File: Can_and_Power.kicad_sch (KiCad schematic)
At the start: 8 parts, among them J2 776280-1, J3 776280-1, U12 MCP2562-E_SN, U3 MCP2562-E_SN

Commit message: Finished routing
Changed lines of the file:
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@@
+	(wire
+		(pts
+			(xy 68.58 45.72) (xy 67.31 45.72)
+		)
+		(stroke
+			(width 0)
+			(type default)
+		)
+	)
 	(wire
 		(pts
@@
 	(symbol
 		(lib_id "power:PWR_FLAG")
-		(at 67.31 45.72 270)
+		(at 68.58 45.72 270)
 		(unit 1)
 		(exclude_from_sim no)
@@
 		(fields_autoplaced yes)
 		(property "Reference" "#FLG02"
-			(at 69.215 45.72 0)
+			(at 70.485 45.72 0)
 			(effects
 				(font
@@
 		)
 		(property "Value" "PWR_FLAG"
-			(at 71.12 45.7199 90)
+			(at 72.39 45.7199 90)
 			(effects
 				(font
@@
 		)
 		(property "Footprint" ""
-			(at 67.31 45.72 0)
+			(at 68.58 45.72 0)
 			(effects
 				(font
@@
 		)
 		(property "Datasheet" "~"
-			(at 67.31 45.72 0)
+			(at 68.58 45.72 0)
 			(effects
 				(font
@@
 		)
 		(property "Description" "Special symbol for telling ERC where power comes from"
-			(at 67.31 45.72 0)
-			(effects
-				(font
+			(at 68.58 45.72 0)
+			(effects
+				(font

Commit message: Finalized analog components. Everything is done 🙏
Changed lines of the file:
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@@
-	)
-	(junction
-		(at 67.31 45.72)
-		(diameter 0)
-		(color 0 0 0 0)
 	)
 	(junction
@@
 	(wire
 		(pts
-			(xy 68.58 45.72) (xy 67.31 45.72)
-		)
-		(stroke
-			(width 0)
-			(type default)
-		)
-	)
-	(wire
-		(pts
 			(xy 220.98 110.49) (xy 220.98 114.3)
 		)
@@
 	(wire
 		(pts
-			(xy 67.31 45.72) (xy 67.31 54.61)
-		)
-		(stroke
-			(width 0)
-			(type default)
-		)
-	)
-	(wire
-		(pts
 			(xy 121.92 69.85) (xy 121.92 111.76)
 		)
@@
 	(wire
 		(pts
-			(xy 67.31 41.91) (xy 67.31 45.72)
+			(xy 67.31 41.91) (xy 67.31 54.61)
 		)
 		(stroke
@@
 					(unit 1)
 				)
-			)
-		)
-	)
-	(symbol
-		(lib_id "power:PWR_FLAG")
-		(at 68.58 45.72 270)
-		(unit 1)
-		(exclude_from_sim no)
-		(in_bom yes)
-		(on_board yes)
-		(dnp no)
-		(fields_autoplaced yes)
-		(property "Reference" "#FLG02"
-			(at 70.485 45.72 0)
-			(effects
-				(font
-					(size 1.27 1.27)
-				)
-				(hide yes)
-			)
-		)
-		(property "Value" "PWR_FLAG"
-			(at 72.39 45.7199 90)
-			(effects
-				(font
-					(size 1.27 1.27)
-				)
-				(justify left)
-			)
-		)
-		(property "Footprint" ""
-			(at 68.58 45.72 0)
-			(effects
-				(font
-					(size 1.27 1.27)
-				)
-				(hide yes)
-			)
-		)
-		(property "Datasheet" "~"
-			(at 68.58 45.72 0)
-			(effects
-				(font
-					(size 1.27 1.27)
-				)
-				(hide yes)
-			)
-		)
-		(property "Description" "Special symbol for telling ERC where power comes from"
-			(at 68.58 45.72 0)
-			(effects
-				(font
-					(size 1.27 1.27)
-				)
-				(hide yes)
-			)
-		)
-		(pin "1"
-		)
-		(instances
-			(project "Main-Board-V2"
-				(path "/c01682a2-308a-4674-9b8f-80e441c05d08/2eeb5b34-c445-4914-b41b-f611e24c0c64"
-					(reference "#FLG02")
-					(unit 1)
-				)

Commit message: Added fuse, switch to horizontal connecotor, redid all routing
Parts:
- added F1: Fuse, Fuse:Fuse_0805_2012Metric, symbol Device:Fuse
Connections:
- net +12V: now also F1.2; no longer J2.1, J3.1
- new net: F1.1, J2.1, J3.1

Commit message: added LED indicators, fixed footprints
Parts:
- C4, C5, C8, C9: footprint GRT155C80J105KE01J:CAPC1005X55N -> Capacitor_SMD:C_0805_2012Metric
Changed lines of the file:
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@@
 			)
 		)
-		(property "Footprint" "GRT155C80J105KE01J:CAPC1005X55N"
+		(property "Footprint" "Capacitor_SMD:C_0805_2012Metric"
 			(at 233.68 53.6448 0)
 			(effects
@@
 			)
 		)
-		(property "Footprint" "GRT155C80J105KE01J:CAPC1005X55N"
+		(property "Footprint" "Capacitor_SMD:C_0805_2012Metric"
 			(at 240.03 109.5248 0)
 			(effects
@@
 			)
 		)
-		(property "Footprint" "GRT155C80J105KE01J:CAPC1005X55N"
+		(property "Footprint" "Capacitor_SMD:C_0805_2012Metric"
 			(at 245.11 53.6448 0)
 			(effects
@@
 			)
 		)
-		(property "Footprint" "GRT155C80J105KE01J:CAPC1005X55N"
+		(property "Footprint" "Capacitor_SMD:C_0805_2012Metric"
 			(at 228.6 109.5248 0)
 			(effects

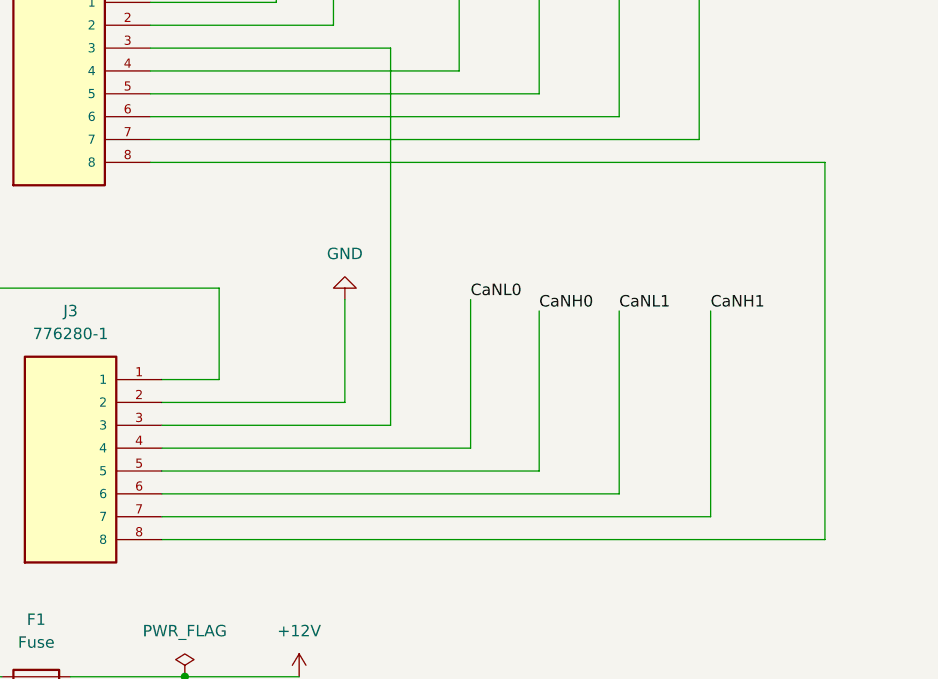
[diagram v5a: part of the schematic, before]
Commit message: redid 35 pos pinout
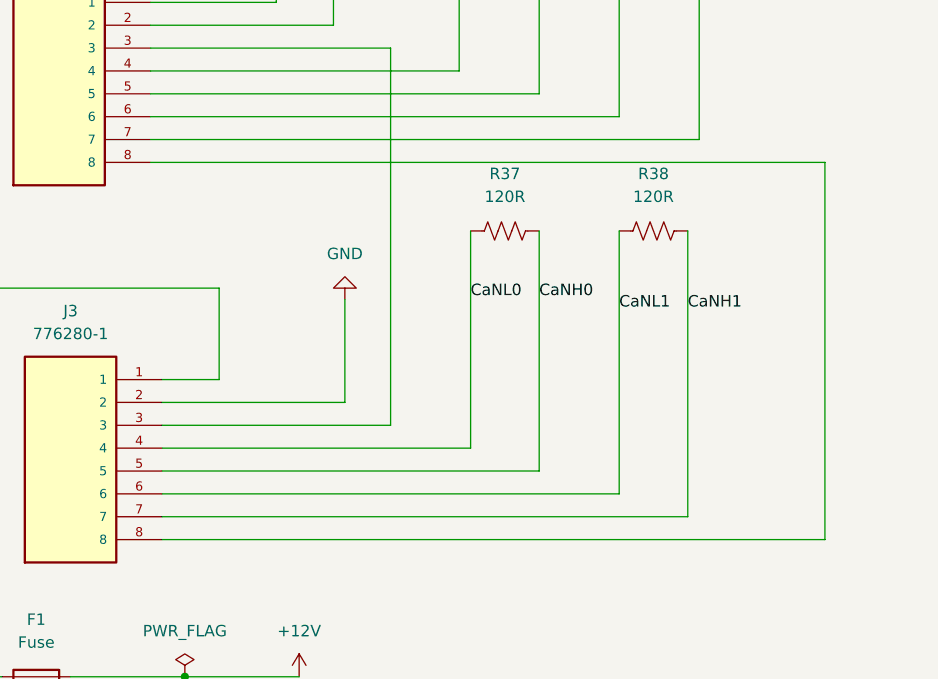
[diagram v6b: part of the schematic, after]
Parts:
- added R37, R38: 120R, Resistor_SMD:R_0805_2012Metric, symbol Device:R_US
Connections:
- net CaNH0: now also R37.2
- net CaNH1: now also R38.2
- net CaNL0: now also R37.1
- net CaNL1: now also R38.1
